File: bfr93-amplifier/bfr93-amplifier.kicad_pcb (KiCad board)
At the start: 2 copper layers, 11 parts, among them J1 IN, J2 PWR, J3 OUT, Q1 BFR93A

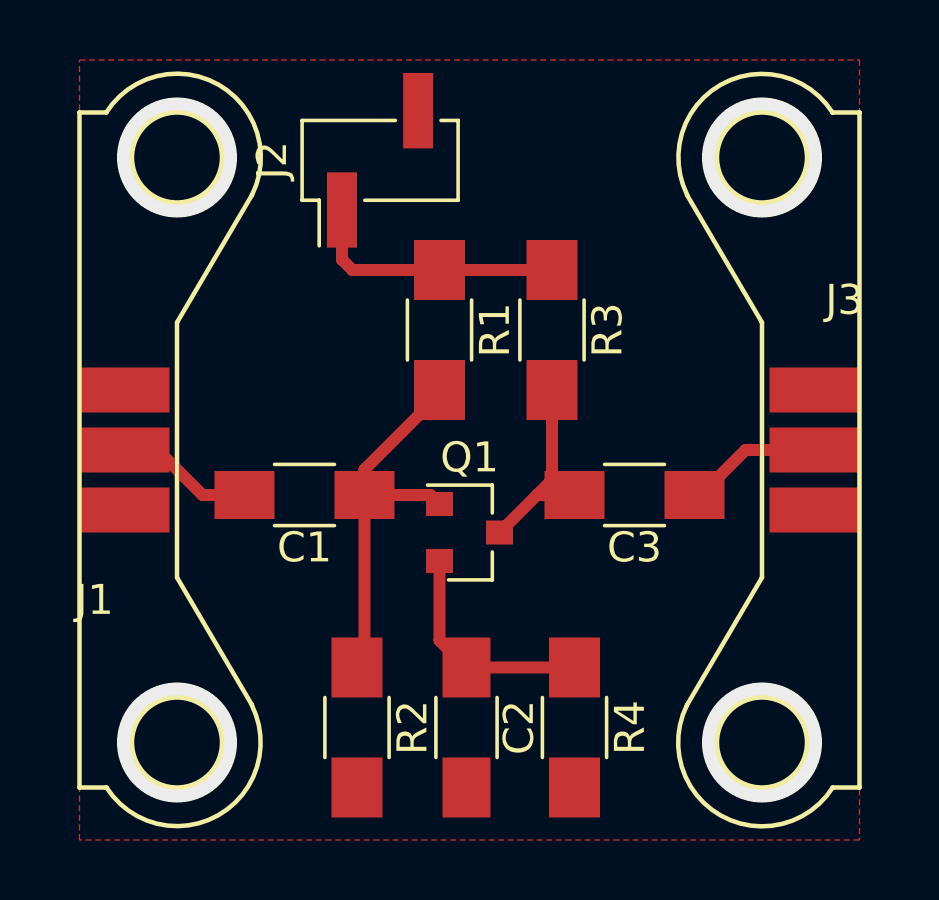
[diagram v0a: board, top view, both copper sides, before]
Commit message: Add power decoupling for amplifier
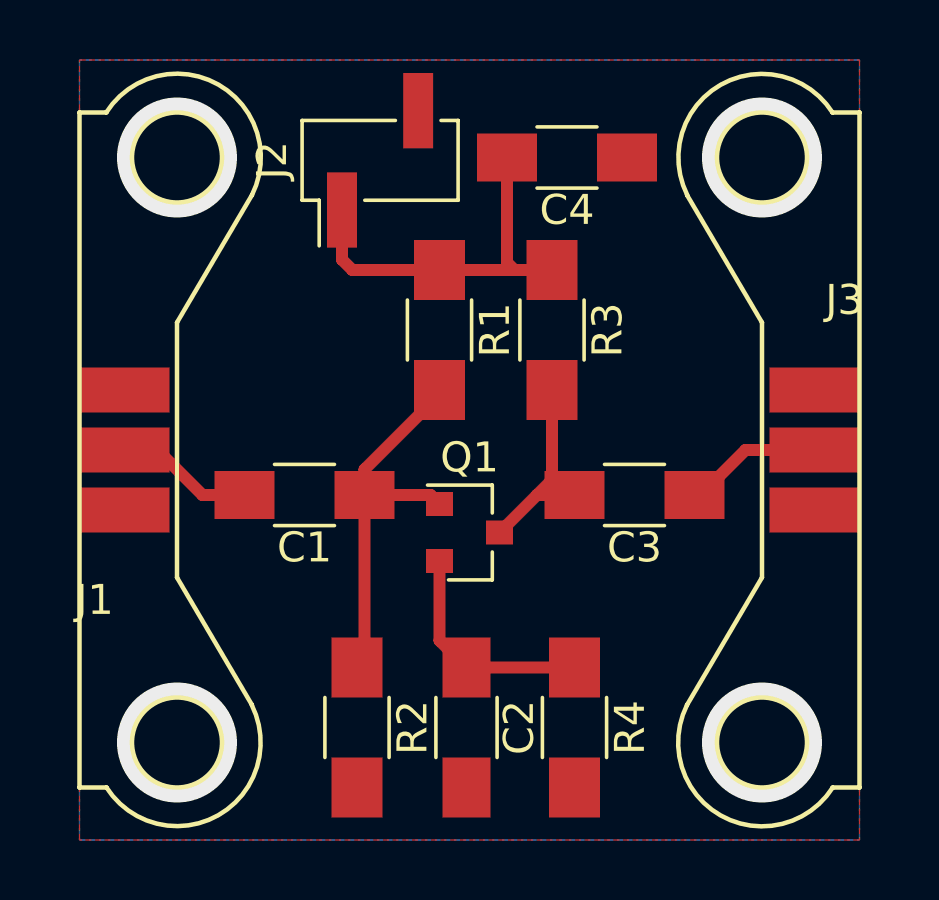
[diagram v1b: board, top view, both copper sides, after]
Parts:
- added C4: 10u, Capacitors_SMD:C_1206_HandSoldering, F.Cu at (61.0, 32.8)
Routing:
- net VCC: track 8.80 -> 13.9 mm
- added copper zone on B.Cu, net Earth
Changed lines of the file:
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@@
     (thickness 1.6)
     (drawings 8)
-    (tracks 30)
+    (tracks 33)
     (zones 0)
-    (modules 11)
+    (modules 12)
     (nets 8)
   )
@@
     (pad_to_mask_clearance 0.2)
     (aux_axis_origin 0 0)
-    (visible_elements FFFFFF7F)
+    (visible_elements 7FFFFFFF)
     (pcbplotparams
       (layerselection 0x010fc_ffffffff)
@@
     )
   )
+  (module Capacitors_SMD:C_1206_HandSoldering (layer F.Cu)
+    (at 61 32.75 180)
+    (descr "Capacitor SMD 1206, hand soldering")
+    (tags "capacitor 1206")
+    (attr smd)
+    (fp_text reference C4 (at 0 -1.75 180) (layer F.SilkS)
+      (effects (font (size 1 1) (thickness 0.15)))
+    )
+    (fp_text value 10u (at 0 2 180) (layer F.Fab)
+      (effects (font (size 1 1) (thickness 0.15)))
+    )
+    (fp_line (start 3.25 1.05) (end -3.25 1.05) (layer F.CrtYd) (width 0.05))
+    (fp_line (start 3.25 1.05) (end 3.25 -1.05) (layer F.CrtYd) (width 0.05))
+    (fp_line (start -3.25 -1.05) (end -3.25 1.05) (layer F.CrtYd) (width 0.05))
+    (fp_line (start -3.25 -1.05) (end 3.25 -1.05) (layer F.CrtYd) (width 0.05))
+    (fp_line (start -1 1.02) (end 1 1.02) (layer F.SilkS) (width 0.12))
+    (fp_line (start 1 -1.02) (end -1 -1.02) (layer F.SilkS) (width 0.12))
+    (fp_line (start -1.6 -0.8) (end 1.6 -0.8) (layer F.Fab) (width 0.1))
+    (fp_line (start 1.6 -0.8) (end 1.6 0.8) (layer F.Fab) (width 0.1))
+    (fp_line (start 1.6 0.8) (end -1.6 0.8) (layer F.Fab) (width 0.1))
+    (fp_line (start -1.6 0.8) (end -1.6 -0.8) (layer F.Fab) (width 0.1))
+    (fp_text user %R (at 0 -1.75 180) (layer F.Fab)
+      (effects (font (size 1 1) (thickness 0.15)))
+    )
+    (pad 2 smd rect (at 2 0 180) (size 2 1.6) (layers F.Cu F.Paste F.Mask)
+      (net 7 VCC))
+    (pad 1 smd rect (at -2 0 180) (size 2 1.6) (layers F.Cu F.Paste F.Mask)
+      (net 3 Earth))
+    (model Capacitors_SMD.3dshapes/C_1206.wrl
+      (at (xyz 0 0 0))
+      (scale (xyz 1 1 1))
+      (rotate (xyz 0 0 0))
+    )
+  )
   (gr_line (start 67.5 55.5) (end 48 55.5) (layer Margin) (width 0.2))
   (gr_arc (start 48 52.25) (end 44.75 52.25) (angle -90) (layer Margin) (width 0.2))
@@
   (gr_line (start 70.75 32.75) (end 70.75 52.25) (layer Margin) (width 0.2))
   (gr_line (start 67.5 29.5) (end 48 29.5) (layer Margin) (width 0.2))
-  (via (at 67.5 32.75) (size 4) (drill 3) (layers F.Cu B.Cu) (net 3))
-  (via (at 67.5 52.25) (size 4) (drill 3) (layers F.Cu B.Cu) (net 3))
-  (via (at 48 52.25) (size 4) (drill 3) (layers F.Cu B.Cu) (net 3))
-  (via (at 48 32.75) (size 4) (drill 3) (layers F.Cu B.Cu) (net 3))
   (segment (start 47.35 42.5) (end 46.25 42.5) (width 0.4) (layer F.Cu) (net 1))
   (segment (start 48.85 44) (end 47.35 42.5) (width 0.4) (layer F.Cu) (net 1))
@@
   (segment (start 56.75 40.65) (end 54.25 43.15) (width 0.4) (layer F.Cu) (net 2))
   (segment (start 56.75 40.5) (end 56.75 40.65) (width 0.4) (layer F.Cu) (net 2))
+  (via (at 67.5 32.75) (size 4) (drill 3) (layers F.Cu B.Cu) (net 3))
+  (via (at 67.5 52.25) (size 4) (drill 3) (layers F.Cu B.Cu) (net 3))
+  (via (at 48 52.25) (size 4) (drill 3) (layers F.Cu B.Cu) (net 3))
+  (via (at 48 32.75) (size 4) (drill 3) (layers F.Cu B.Cu) (net 3))
   (segment (start 56.75 48.85) (end 57.65 49.75) (width 0.4) (layer F.Cu) (net 4))
   (segment (start 56.75 46.2) (end 56.75 48.85) (width 0.4) (layer F.Cu) (net 4))
@@
   (segment (start 53.5 34.5) (end 53.5 36.155) (width 0.4) (layer F.Cu) (net 7))
   (segment (start 56.75 36.5) (end 60.5 36.5) (width 0.4) (layer F.Cu) (net 7))
+  (segment (start 59.25 36.5) (end 60.5 36.5) (width 0.4) (layer F.Cu) (net 7))
+  (segment (start 59 36.25) (end 59.25 36.5) (width 0.4) (layer F.Cu) (net 7))
+  (segment (start 59 32.75) (end 59 36.25) (width 0.4) (layer F.Cu) (net 7))
   (zone (net 3) (net_name Earth) (layer F.Cu) (hatch edge 0.508)
     (connect_pads yes (clearance 0.3))
@@
       )
     )
+  )
+  (zone (net 3) (net_name Earth) (layer B.Cu) (hatch edge 0.508)
+    (connect_pads yes (clearance 0.3))
+    (min_thickness 0.25)
+    (fill yes (arc_segments 16) (thermal_gap 0.508) (thermal_bridge_width 0.508) (smoothing fillet) (radius 3))
+    (polygon
+      (pts
+        (xy 70.75 29.5) (xy 44.75 29.5) (xy 44.75 55.5) (xy 70.75 55.5)
+      )
+    )
